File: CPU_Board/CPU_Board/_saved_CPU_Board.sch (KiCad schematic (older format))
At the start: 110 parts, among them J101 Screw_Terminal_01x03, J102 Conn_02x01, J103 Conn_02x01, J104 Conn_01x08_Male, J105 Conn_02x09_Odd_Even, J106 Micro_SD_Card_Det, J107 Conn_01x06_Male, J108 Conn_02x01, J109 Conn_02x01, J110 Screw_Terminal_01x04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

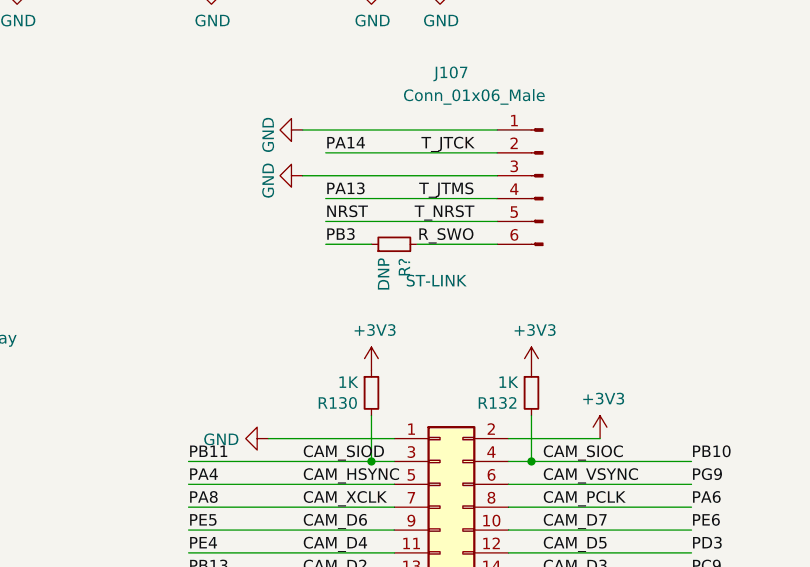
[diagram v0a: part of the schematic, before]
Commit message: RAM (55mm) und SDCARD (65 mm) length gematcht, fehlt noch DCMI
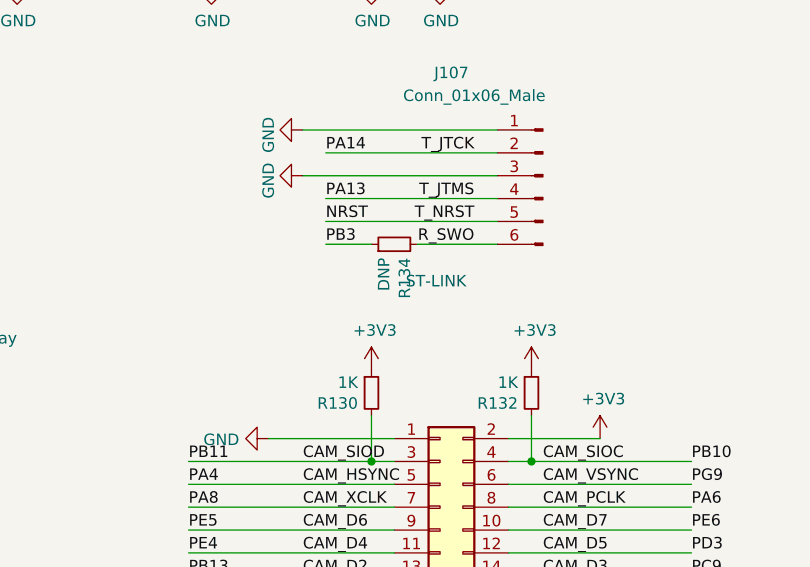
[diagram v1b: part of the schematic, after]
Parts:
- gave numbers to parts that had none: 1
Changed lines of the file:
@@
 P 14100 5450
 AR Path="/5FDD0F66/600784DB" Ref="R?"  Part="1"
-AR Path="/600784DB" Ref="R?"  Part="1"
-F 0 "R?" H 14041 5404 50  0000 R CNN
+AR Path="/600784DB" Ref="R134"  Part="1"
+F 0 "R134" H 14041 5404 50  0000 R CNN
 F 1 "DNP" H 14041 5495 50  0000 R CNN
 F 2 "Resistor_SMD:R_0603_1608Metric" H 14100 5450 50  0001 C CNN
